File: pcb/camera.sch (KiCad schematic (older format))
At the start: 3 parts, among them IC3 SI2302CDS, IC4 SI2302CDS, J1 AUDIO-JACK2.5MM

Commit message: Changed camera interface to use optocouplers
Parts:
- removed IC3, IC4: SI2302CDS, SOT95P237X112-3N, symbol SI2302CDS-T1-GE3:SI2302CDS-T1-GE3
- added IC3, IC4: EL817S, EL817S, symbol EL817S
- added R25, R26: 150, symbol R
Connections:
- net labels added: Earth
- wire segments 17 -> 19
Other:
- note added: "Optocoupler based camera interface\nWorks with Canon/Nikon/Fuji/Sony/Pentax/Sigma/Hasselblad/Olympus\nDoes not work with Panasonic"
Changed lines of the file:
@@
 LIBS:ab2_usb
 LIBS:ab2_xtal
+LIBS:EL817S
 LIBS:pir-cache
 EELAYER 25 0
@@
 $Descr A4 11693 8268
 encoding utf-8
-Sheet 5 6
+Sheet 4 6
 Title ""
 Date ""
@@
 Comment4 ""
 $EndDescr
-Text HLabel 5300 2050 0    60   Input ~ 0
+Text HLabel 4650 2050 0    60   Input ~ 0
 FOCUS
-Text HLabel 5250 3250 0    60   Input ~ 0
-SHUTTER
 $Comp
 L AUDIO-JACK2.5MM J1
@@
 F 3 "" H 1900 2500 60  0001 C CNN
 	1    1900 2500
-	1    0    0    -1
-$EndComp
-$Comp
-L SI2302CDS-T1-GE3:SI2302CDS-T1-GE3 IC4
-U 1 1 5A804D7D
-P 5600 2050
-F 0 "IC4" H 6250 2350 50  0000 L CNN
-F 1 "SI2302CDS" H 6250 2250 50  0000 L CNN
-F 2 "SOT95P237X112-3N" H 6250 2150 50  0001 L CNN
-F 3 "http://www.vishay.com/docs/68645/si2302cd.pdf" H 6250 2050 50  0001 L CNN
-F 4 "SI2302CDS-T1-GE3, N-channel MOSFET Transistor 2.6 A 20 V, 3-Pin SOT-23" H 6250 1950 50  0001 L CNN "Description"
-F 5 "Vishay" H 6250 1850 50  0001 L CNN "Manufacturer_Name"
-F 6 "SI2302CDS-T1-GE3" H 6250 1750 50  0001 L CNN "Manufacturer_Part_Number"
-F 7 "RS" H 6250 1650 50  0001 L CNN "Supplier_Name"
-F 8 "7103232P" H 6250 1550 50  0001 L CNN "RS Part Number"
-F 9 "1.12" H 6250 1450 50  0001 L CNN "Height"
-	1    5600 2050
 	1    0    0    -1
 $EndComp
@@
 Wire Wire Line
 	5300 2050 5600 2050
-Text GLabel 6800 2050 2    60   Input ~ 0
+Text GLabel 7500 2050 2    60   Input ~ 0
 RING
 Wire Wire Line
-	6400 2050 6800 2050
-Text GLabel 6800 2350 2    60   Input ~ 0
+	7100 2050 7500 2050
+Text GLabel 7850 2150 2    60   Input ~ 0
 SHIELD
-Wire Wire Line
-	5600 2150 5500 2150
-Wire Wire Line
-	5500 2150 5500 2350
-Wire Wire Line
-	5500 2350 6800 2350
 $Comp
-L SI2302CDS-T1-GE3:SI2302CDS-T1-GE3 IC3
-U 1 1 5A805147
-P 5550 3250
-F 0 "IC3" H 6200 3550 50  0000 L CNN
-F 1 "SI2302CDS" H 6200 3450 50  0000 L CNN
-F 2 "SOT95P237X112-3N" H 6200 3350 50  0001 L CNN
-F 3 "http://www.vishay.com/docs/68645/si2302cd.pdf" H 6200 3250 50  0001 L CNN
-F 4 "SI2302CDS-T1-GE3, N-channel MOSFET Transistor 2.6 A 20 V, 3-Pin SOT-23" H 6200 3150 50  0001 L CNN "Description"
-F 5 "Vishay" H 6200 3050 50  0001 L CNN "Manufacturer_Name"
-F 6 "SI2302CDS-T1-GE3" H 6200 2950 50  0001 L CNN "Manufacturer_Part_Number"
-F 7 "RS" H 6200 2850 50  0001 L CNN "Supplier_Name"
-F 8 "7103232P" H 6200 2750 50  0001 L CNN "RS Part Number"
-F 9 "1.12" H 6200 2650 50  0001 L CNN "Height"
-	1    5550 3250
+L EL817S IC3
+U 1 1 5A80CC0F
+P 5600 2050
+F 0 "IC3" H 6950 2350 50  0000 L CNN
+F 1 "EL817S" H 6950 2250 50  0000 L CNN
+F 2 "EL817S" H 6950 2150 50  0001 L CNN
+F 3 "http://www.mouser.com/ds/2/143/201407061833256242-365628.pdf" H 6950 2050 50  0001 L CNN
+F 4 "Transistor Output Optocouplers Photo-Coupler" H 6950 1950 50  0001 L CNN "Description"
+F 5 "Everlight" H 6950 1850 50  0001 L CNN "Manufacturer_Name"
+F 6 "EL817S" H 6950 1750 50  0001 L CNN "Manufacturer_Part_Number"
+F 7 "RS" H 6950 1650 50  0001 L CNN "Supplier_Name"
+F 8 "" H 6950 1550 50  0001 L CNN "RS Part Number"
+F 9 "" H 6950 1450 50  0001 L CNN "Height"
+	1    5600 2050
+	1    0    0    -1
+$EndComp
+$Comp
+L Earth #PWR13
+U 1 1 5A80CEBC
+P 5500 2300
+F 0 "#PWR13" H 5500 2050 50  0001 C CNN
+F 1 "Earth" H 5500 2150 50  0001 C CNN
+F 2 "" H 5500 2300 50  0001 C CNN
+F 3 "" H 5500 2300 50  0001 C CNN
+	1    5500 2300
 	1    0    0    -1
 $EndComp
 Wire Wire Line
-	5250 3250 5550 3250
-Text GLabel 6750 3250 2    60   Input ~ 0
+	5500 2300 5500 2150
+Wire Wire Line
+	5500 2150 5600 2150
+Wire Wire Line
+	7100 2150 7850 2150
+$Comp
+L R R25
+U 1 1 5A80CFBA
+P 5150 2050
+F 0 "R25" V 5230 2050 50  0000 C CNN
+F 1 "150" V 5150 2050 50  0000 C CNN
+F 2 "" V 5080 2050 50  0001 C CNN
+F 3 "" H 5150 2050 50  0001 C CNN
+	1    5150 2050
+	0    1    1    0
+$EndComp
+Wire Wire Line
+	4650 2050 5000 2050
+Text HLabel 4650 3200 0    60   Input ~ 0
+SHUTTER
+Wire Wire Line
+	5300 3200 5600 3200
+Text GLabel 7500 3200 2    60   Input ~ 0
 TIP
 Wire Wire Line
-	6350 3250 6750 3250
-Text GLabel 6750 3550 2    60   Input ~ 0
+	7100 3200 7500 3200
+Text GLabel 7850 3300 2    60   Input ~ 0
 SHIELD
+$Comp
+L EL817S IC4
+U 1 1 5A80D1A3
+P 5600 3200
+F 0 "IC4" H 6950 3500 50  0000 L CNN
+F 1 "EL817S" H 6950 3400 50  0000 L CNN
+F 2 "EL817S" H 6950 3300 50  0001 L CNN
+F 3 "http://www.mouser.com/ds/2/143/201407061833256242-365628.pdf" H 6950 3200 50  0001 L CNN
+F 4 "Transistor Output Optocouplers Photo-Coupler" H 6950 3100 50  0001 L CNN "Description"
+F 5 "Everlight" H 6950 3000 50  0001 L CNN "Manufacturer_Name"
+F 6 "EL817S" H 6950 2900 50  0001 L CNN "Manufacturer_Part_Number"
+F 7 "RS" H 6950 2800 50  0001 L CNN "Supplier_Name"
+F 8 "" H 6950 2700 50  0001 L CNN "RS Part Number"
+F 9 "" H 6950 2600 50  0001 L CNN "Height"
+	1    5600 3200
+	1    0    0    -1
+$EndComp
+$Comp
+L Earth #PWR14
+U 1 1 5A80D1A9
+P 5500 3450
+F 0 "#PWR14" H 5500 3200 50  0001 C CNN
+F 1 "Earth" H 5500 3300 50  0001 C CNN
+F 2 "" H 5500 3450 50  0001 C CNN
+F 3 "" H 5500 3450 50  0001 C CNN
+	1    5500 3450
+	1    0    0    -1
+$EndComp
 Wire Wire Line
-	5550 3350 5450 3350
+	5500 3450 5500 3300
 Wire Wire Line
-	5450 3350 5450 3550
+	5500 3300 5600 3300
 Wire Wire Line
-	5450 3550 6750 3550
+	7100 3300 7850 3300
+$Comp
+L R R26
+U 1 1 5A80D1B2
+P 5150 3200
+F 0 "R26" V 5230 3200 50  0000 C CNN
+F 1 "150" V 5150 3200 50  0000 C CNN
+F 2 "" V 5080 3200 50  0001 C CNN
+F 3 "" H 5150 3200 50  0001 C CNN
+	1    5150 3200
+	0    1    1    0
+$EndComp
+Wire Wire Line
+	4650 3200 5000 3200
+Text Notes 4800 1550 0    60   ~ 0
+Optocoupler based camera interface\nWorks with Canon/Nikon/Fuji/Sony/Pentax/Sigma/Hasselblad/Olympus\nDoes not work with Panasonic
 $EndSCHEMATC

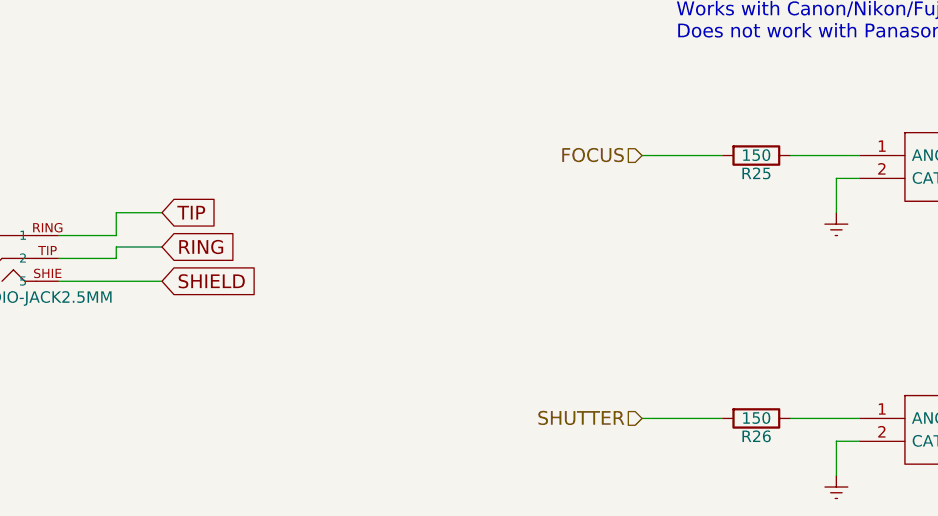
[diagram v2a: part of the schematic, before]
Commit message: Added testpoints
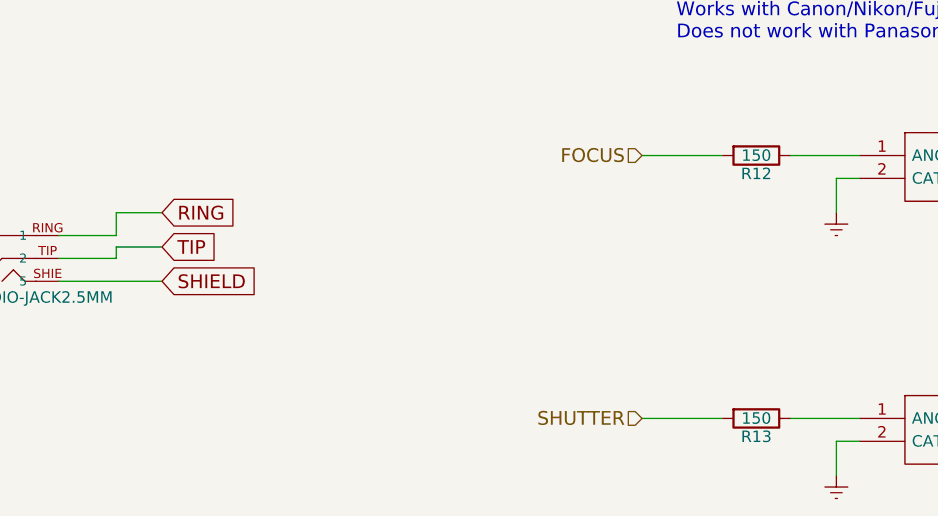
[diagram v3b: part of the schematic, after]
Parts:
- renumbered R25 to R12, R26 to R13
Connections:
- net RING: now also J1.RING (1); no longer J1.TIP (2)
- net TIP: now also J1.TIP (2); no longer J1.RING (1)
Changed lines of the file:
@@
 Text GLabel 2550 2600 2    60   Input ~ 0
 SHIELD
+Text GLabel 2550 2300 2    60   Input ~ 0
+RING
 Text GLabel 2550 2450 2    60   Input ~ 0
-RING
-Text GLabel 2550 2300 2    60   Input ~ 0
 TIP
 Wire Wire Line
@@
 $EndComp
 $Comp
-L Earth #PWR013
+L Earth #PWR13
 U 1 1 5A80CEBC
 P 5500 2300
-F 0 "#PWR013" H 5500 2050 50  0001 C CNN
+F 0 "#PWR13" H 5500 2050 50  0001 C CNN
 F 1 "Earth" H 5500 2150 50  0001 C CNN
 F 2 "" H 5500 2300 50  0001 C CNN
@@
 	7100 2150 7850 2150
 $Comp
-L R R25
+L R R12
 U 1 1 5A80CFBA
 P 5150 2050
-F 0 "R25" V 5230 2050 50  0000 C CNN
+F 0 "R12" V 5230 2050 50  0000 C CNN
 F 1 "150" V 5150 2050 50  0000 C CNN
 F 2 "" V 5080 2050 50  0001 C CNN
@@
 $EndComp
 $Comp
-L Earth #PWR014
+L Earth #PWR14
 U 1 1 5A80D1A9
 P 5500 3450
-F 0 "#PWR014" H 5500 3200 50  0001 C CNN
+F 0 "#PWR14" H 5500 3200 50  0001 C CNN
 F 1 "Earth" H 5500 3300 50  0001 C CNN
 F 2 "" H 5500 3450 50  0001 C CNN
@@
 	7100 3300 7850 3300
 $Comp
-L R R26
+L R R13
 U 1 1 5A80D1B2
 P 5150 3200
-F 0 "R26" V 5230 3200 50  0000 C CNN
+F 0 "R13" V 5230 3200 50  0000 C CNN
 F 1 "150" V 5150 3200 50  0000 C CNN
 F 2 "" V 5080 3200 50  0001 C CNN

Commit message: Assigned footprints to all components
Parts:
- IC3, IC4: footprint EL817S -> EL817S:EL817S
- R12, R13: footprint (none) -> Resistors_SMD:R_1210
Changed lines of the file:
@@
 F 0 "IC3" H 6950 2350 50  0000 L CNN
 F 1 "EL817S" H 6950 2250 50  0000 L CNN
-F 2 "EL817S" H 6950 2150 50  0001 L CNN
+F 2 "EL817S:EL817S" H 6950 2150 50  0001 L CNN
 F 3 "http://www.mouser.com/ds/2/143/201407061833256242-365628.pdf" H 6950 2050 50  0001 L CNN
 F 4 "Transistor Output Optocouplers Photo-Coupler" H 6950 1950 50  0001 L CNN "Description"
@@
 F 0 "R12" V 5230 2050 50  0000 C CNN
 F 1 "150" V 5150 2050 50  0000 C CNN
-F 2 "" V 5080 2050 50  0001 C CNN
+F 2 "Resistors_SMD:R_1210" V 5080 2050 50  0001 C CNN
 F 3 "" H 5150 2050 50  0001 C CNN
 	1    5150 2050
@@
 F 0 "IC4" H 6950 3500 50  0000 L CNN
 F 1 "EL817S" H 6950 3400 50  0000 L CNN
-F 2 "EL817S" H 6950 3300 50  0001 L CNN
+F 2 "EL817S:EL817S" H 6950 3300 50  0001 L CNN
 F 3 "http://www.mouser.com/ds/2/143/201407061833256242-365628.pdf" H 6950 3200 50  0001 L CNN
 F 4 "Transistor Output Optocouplers Photo-Coupler" H 6950 3100 50  0001 L CNN "Description"
@@
 F 0 "R13" V 5230 3200 50  0000 C CNN
 F 1 "150" V 5150 3200 50  0000 C CNN
-F 2 "" V 5080 3200 50  0001 C CNN
+F 2 "Resistors_SMD:R_1210" V 5080 3200 50  0001 C CNN
 F 3 "" H 5150 3200 50  0001 C CNN
 	1    5150 3200

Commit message: Put the first components on layout
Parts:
- J1: footprint SparkFun-STEREOJACK2.5MM_STEREOJACK2.5MM -> (none)
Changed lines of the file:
@@
 F 0 "J1" H 1700 2620 50  0000 L BNN
 F 1 "AUDIO-JACK2.5MM" H 1700 2300 50  0000 L BNN
-F 2 "SparkFun-STEREOJACK2.5MM_STEREOJACK2.5MM" H 2000 2250 50  0001 C CNN
+F 2 "" H 2000 2250 50  0001 C CNN
 F 3 "" H 1900 2500 60  0001 C CNN
 	1    1900 2500

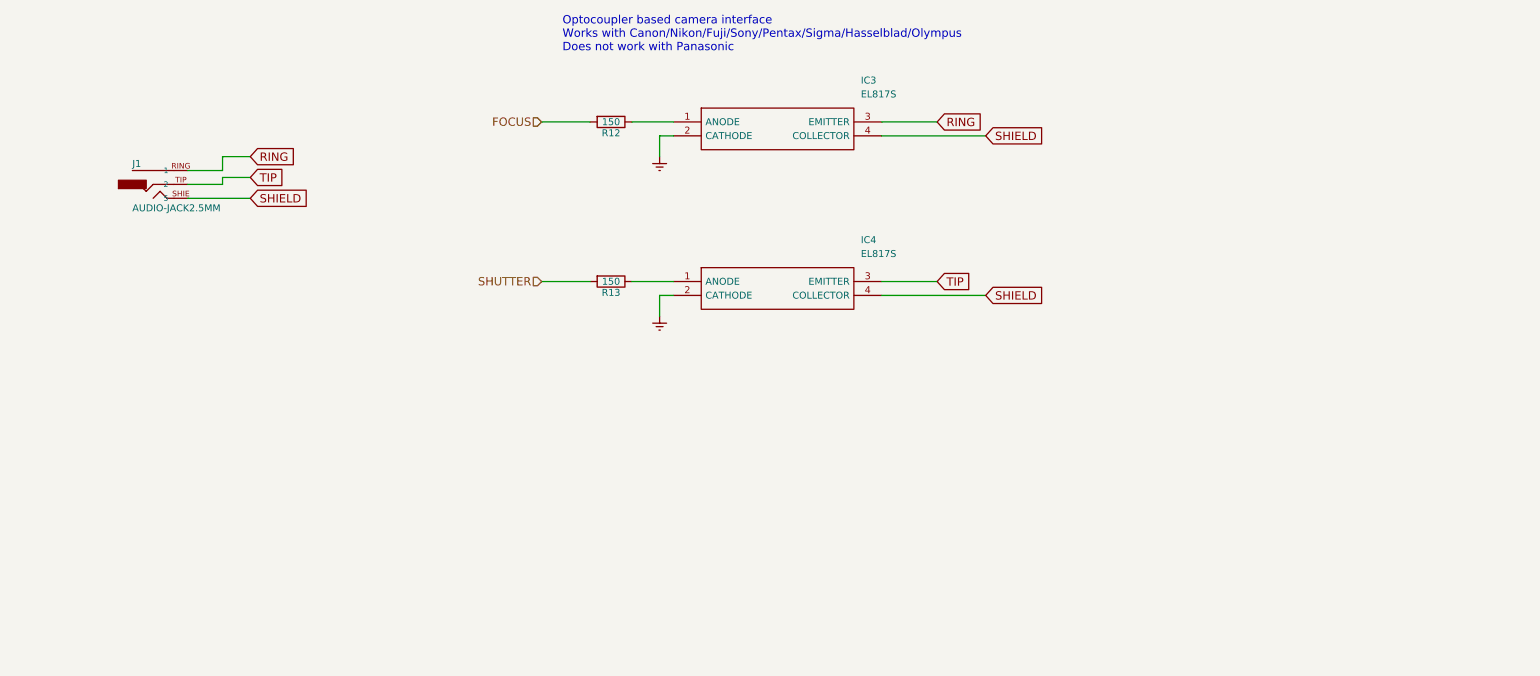
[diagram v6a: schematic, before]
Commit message: I think I found a way to have Panasonic interface
Uses 2 more optocouplers, 3 more diodes and some current limiting
resistors.
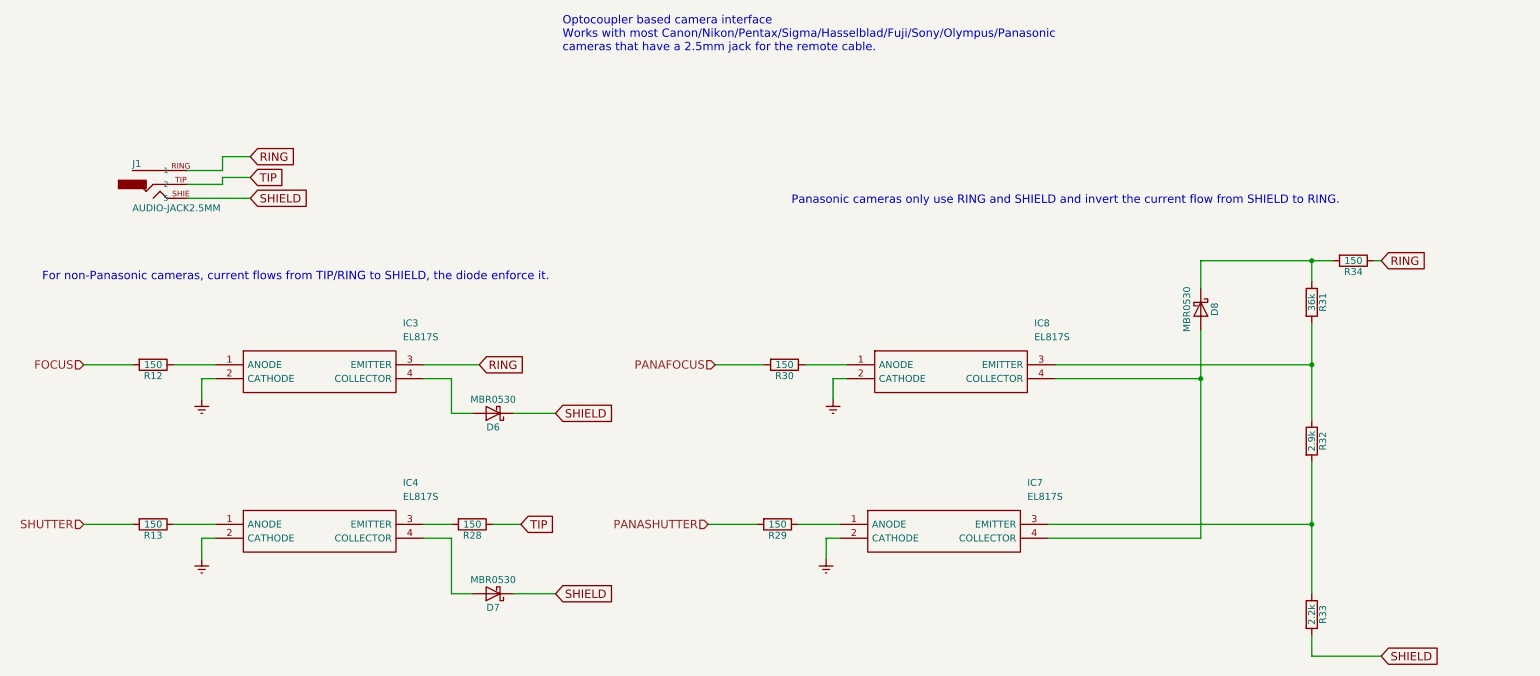
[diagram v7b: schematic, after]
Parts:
- added D6, D7, D8: MBR0530, Diodes_SMD:SOD-123, symbol MBR0530
- added IC7, IC8: EL817S, EL817S:EL817S, symbol EL817S
- added R28, R29, R30, R34: 150, Resistors_SMD:R_1210, symbol R
- added R31: 36k, symbol R
- added R32: 2.9k, symbol R
- added R33: 2.2k, symbol R
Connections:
- net Earth: now also IC7.2 (CATHODE), IC8.2 (CATHODE)
- net RING: now also R34.1
- net SHIELD: now also D6.1 (K), D7.1 (K), R33.2; no longer IC3.4 (COLLECTOR), IC4.4 (COLLECTOR)
- net TIP: now also R28.1; no longer IC4.3 (EMITTER)
- new net: D6.2 (A), IC3.4 (COLLECTOR)
- new net: IC4.3 (EMITTER), R28.2
- new net: D7.2 (A), IC4.4 (COLLECTOR)
- new net: IC8.1 (ANODE), R30.1
- new net: IC8.3 (EMITTER), R31.2, R32.1
- new net: D8.2 (A), IC7.4 (COLLECTOR), IC8.4 (COLLECTOR)
- new net: IC7.1 (ANODE), R29.1
- new net: IC7.3 (EMITTER), R32.2, R33.1
- new net: D8.1 (K), R31.1, R34.2
- new net PANAFOCUS: R30.2
- new net PANASHUTTER: R29.2
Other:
- note added: "For non-Panasonic cameras, current flows from TIP/RING to SHIELD, the diode enforce it."
- note added: "Optocoupler based camera interface\nWorks with most Canon/Nikon/Pentax/Sigma/Hasselblad/Fuji/Sony/Olympus/Panasonic \ncameras that have a 2.5mm jack for the remote cable."
- note added: "Panasonic cameras only use RING and SHIELD and invert the current flow from SHIELD to RING."
- note removed: "Optocoupler based camera interface\nWorks with Canon/Nikon/Fuji/Sony/Pentax/Sigma/Hasselblad/Olympus\nDoes not work with Panasonic"
- moved on the sheet: IC3, IC4, R12, R13

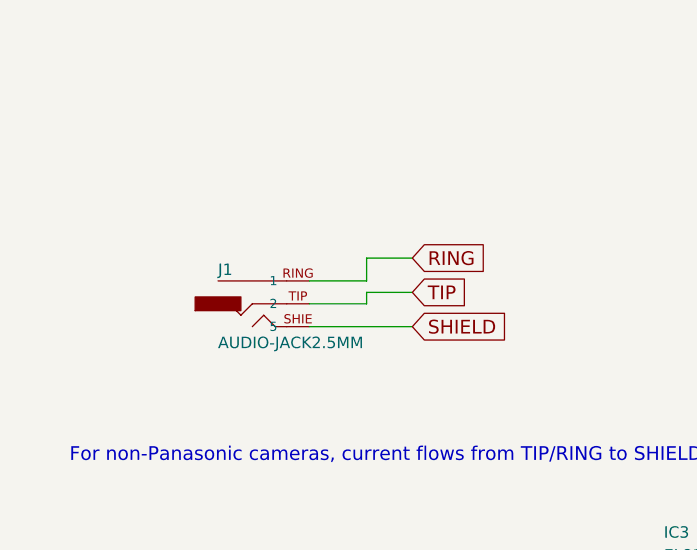
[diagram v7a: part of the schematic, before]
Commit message: Reassigned some footprints, added some libraries
Normally I can start working on PCB.
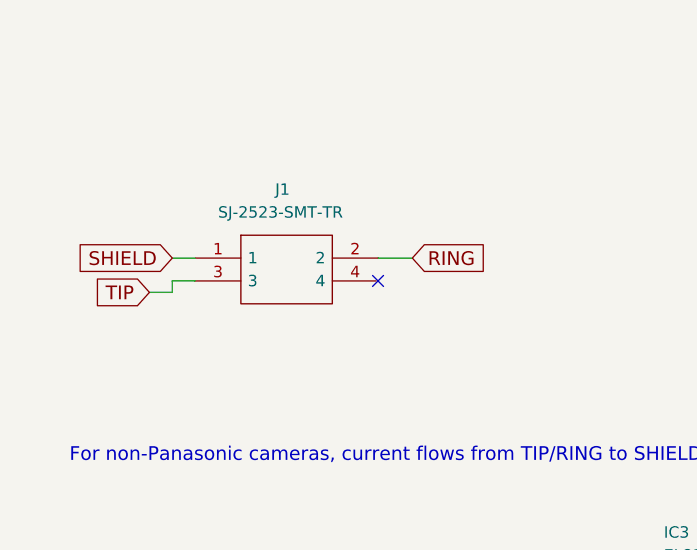
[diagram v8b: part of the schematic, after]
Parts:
- removed J1: AUDIO-JACK2.5MM, symbol AUDIO-JACK2.5MM
- added J1: SJ-2523-SMT-TR, SJ-2523-SMT-TR:SJ-2523-SMT-TR, symbol SJ-2523-SMT-TR
- D6, D7, D8: footprint Diodes_SMD:SOD-123 -> MBR0530:SOD3716X135N
- R12, R13, R28, R29, R30, R34: footprint Resistors_SMD:R_1210 -> Resistors_SMD:R_1206
- R31, R32, R33: footprint (none) -> Resistors_SMD:R_1206
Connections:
- net RING: now also J1.2
- net SHIELD: now also J1.1
- net TIP: now also J1.3
- no-connect marks 0 -> 1
